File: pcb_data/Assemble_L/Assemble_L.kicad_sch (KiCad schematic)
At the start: 75 parts, among them U1 XIAO-nRF52840

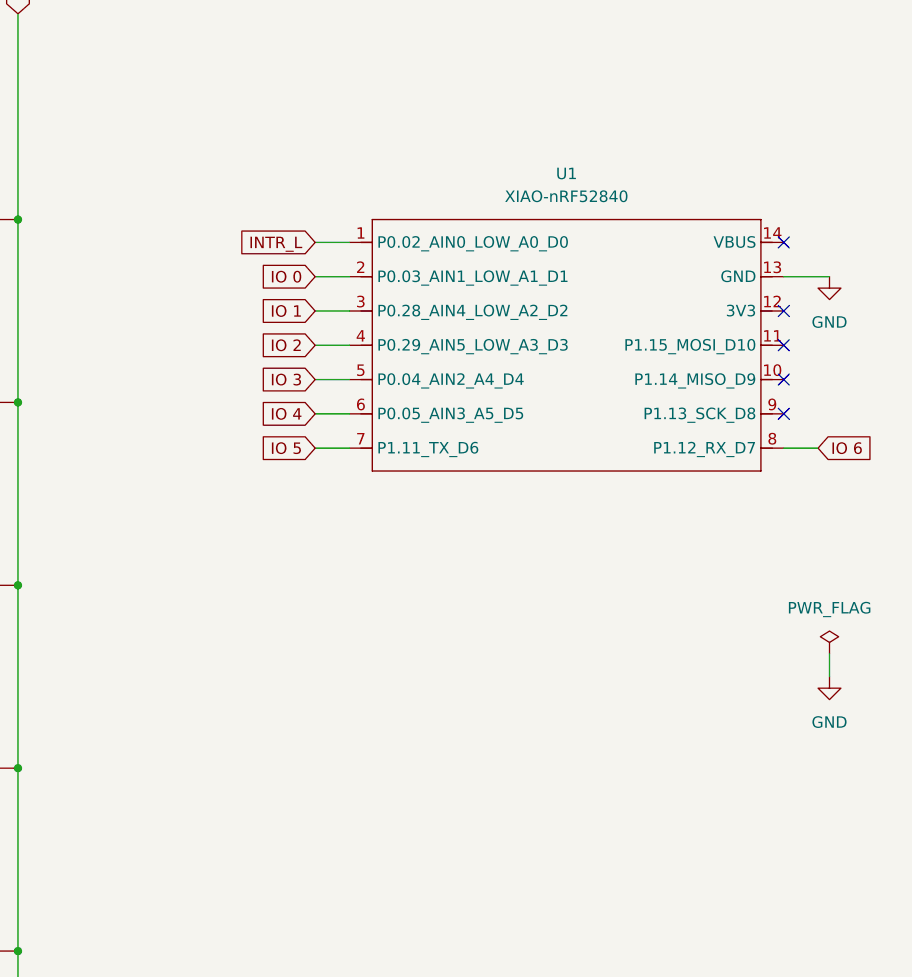
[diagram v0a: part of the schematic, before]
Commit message: replace symbol of xiao-ble
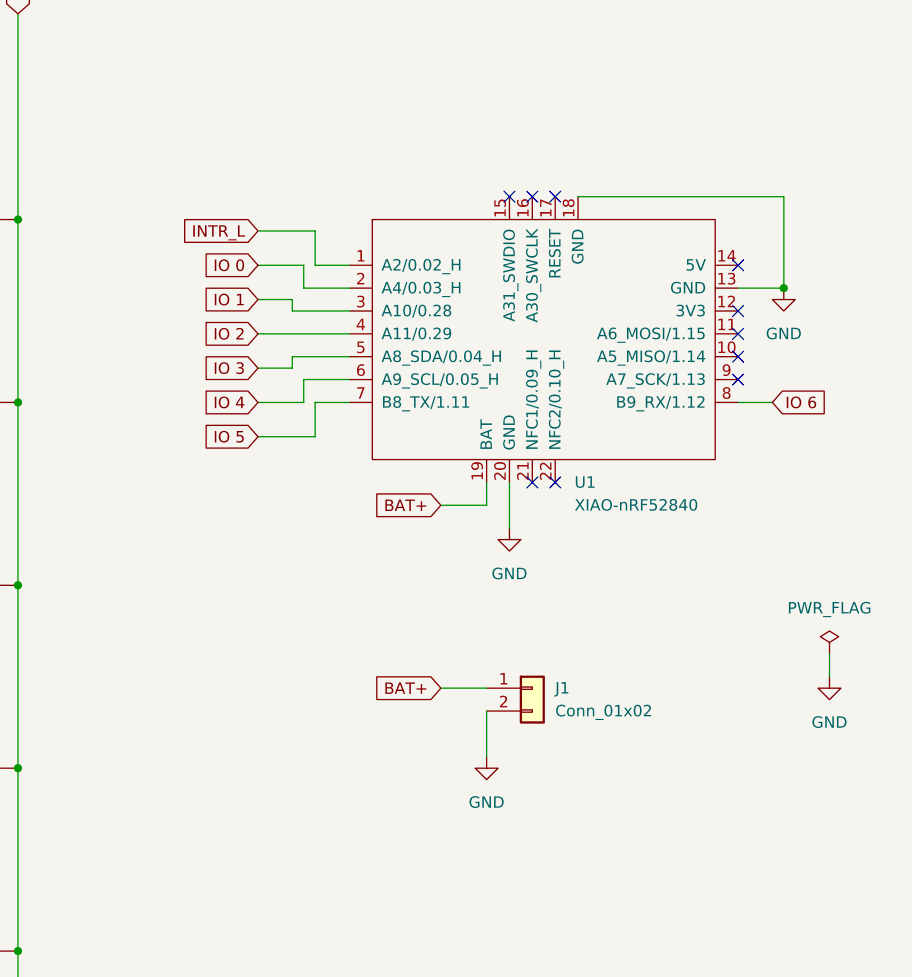
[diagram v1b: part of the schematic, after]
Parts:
- added J1: Conn_01x02, Connector_JST:JST_PH_B2B-PH-K_1x02_P2.00mm_Vertical, symbol Connector_Generic:Conn_01x02
- U1: symbol Seeed_Studio_XIAO_Series:XIAO-nRF52840-DIP -> mcu:xiao-ble
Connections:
- net GND: now also U1.18 (GND), U1.20 (GND), J1.2 (Pin_2)
- new net BAT+: J1.1 (Pin_1), U1.19 (BAT)
- no-connect marks 5 -> 10
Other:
- moved on the sheet: U1
